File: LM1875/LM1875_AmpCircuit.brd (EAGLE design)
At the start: 59.4 x 31.7 mm, 16 parts, among them X1 22-23-2031, X2 22-23-2021, X3 22-23-2021

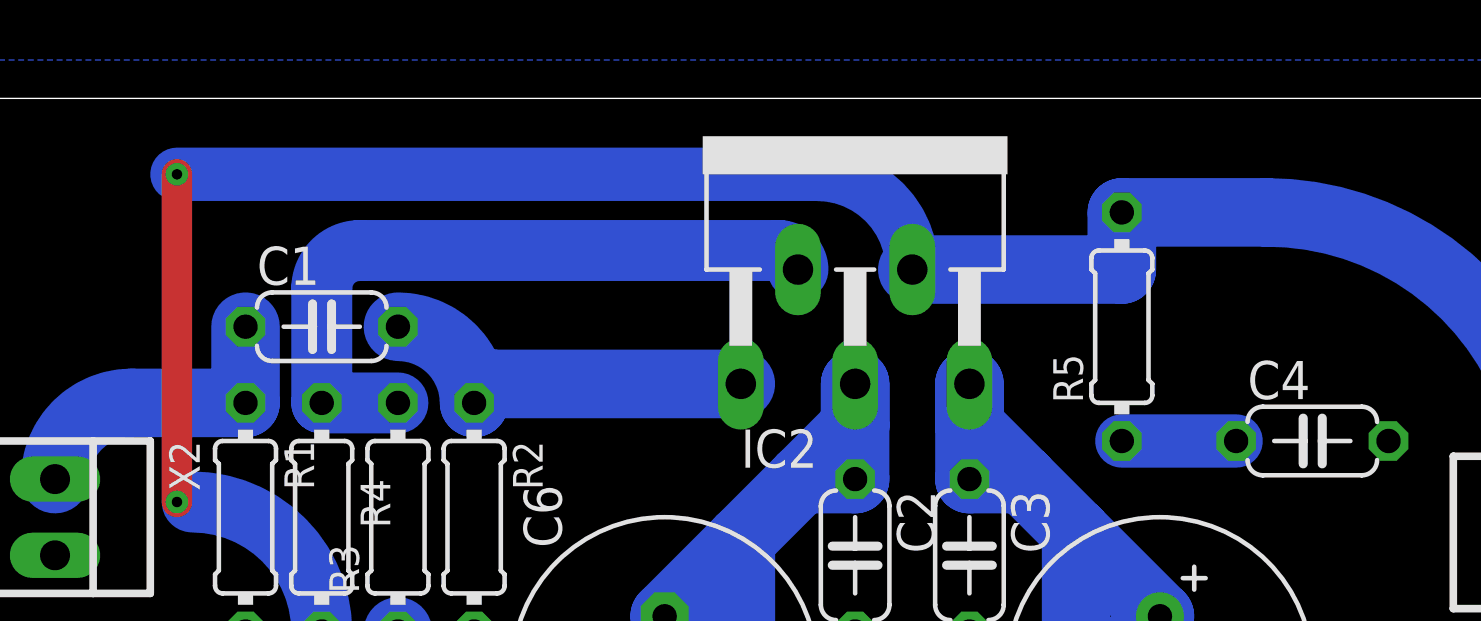
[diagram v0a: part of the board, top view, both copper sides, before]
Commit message: Edited the layout for better noise rejection
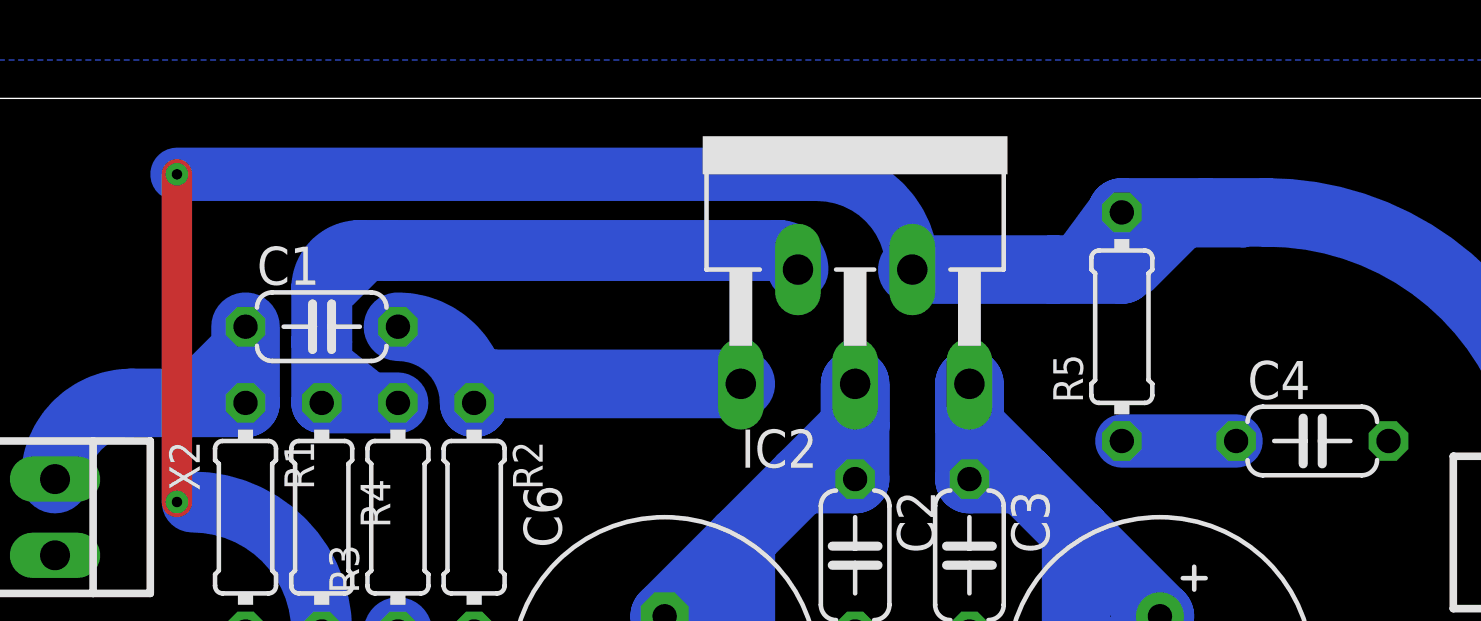
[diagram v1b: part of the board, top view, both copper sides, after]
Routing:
- net N$5: track 81.0 -> 100.2 mm
- net N$4: track 25.7 -> 31.1 mm
- net N$1: track 13.5 -> 15.9 mm
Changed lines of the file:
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@@
 <wire x1="30.48" y1="73.66" x2="31.75" y2="74.93" width="1.016" layer="16" curve="-90"/>
 <wire x1="45.72" y1="74.93" x2="46.355" y2="74.295" width="1.016" layer="16" curve="-90"/>
-<wire x1="30.48" y1="69.85" x2="30.48" y2="73.66" width="2.032" layer="16"/>
+<wire x1="30.48" y1="69.85" x2="30.48" y2="71.882" width="2.032" layer="16"/>
+<wire x1="30.48" y1="71.882" x2="30.48" y2="73.66" width="2.032" layer="16"/>
 <wire x1="30.48" y1="73.66" x2="31.75" y2="74.93" width="2.032" layer="16" curve="-90"/>
 <wire x1="46.355" y1="74.295" x2="45.72" y2="74.93" width="2.032" layer="16" curve="90"/>
-<wire x1="45.72" y1="74.93" x2="31.75" y2="74.93" width="2.032" layer="16"/>
+<wire x1="45.72" y1="74.93" x2="32.766" y2="74.93" width="2.032" layer="16"/>
+<wire x1="32.766" y1="74.93" x2="31.75" y2="74.93" width="2.032" layer="16"/>
 <wire x1="30.48" y1="69.85" x2="33.02" y2="69.85" width="2.032" layer="16"/>
+<wire x1="30.48" y1="71.882" x2="33.02" y2="69.85" width="0.8128" layer="16"/>
+<wire x1="32.766" y1="74.93" x2="31.242" y2="73.406" width="0.8128" layer="16"/>
 </signal>
 <signal name="N$5">
@@
 <via x="25.654" y="66.548" extent="1-16" drill="0.35"/>
 <wire x1="25.654" y1="77.47" x2="25.654" y2="66.548" width="1.016" layer="1"/>
-<wire x1="50.165" y1="74.295" x2="57.15" y2="74.295" width="2.286" layer="16"/>
+<wire x1="50.165" y1="74.295" x2="54.864" y2="74.295" width="2.286" layer="16"/>
+<wire x1="54.864" y1="74.295" x2="57.15" y2="74.295" width="2.286" layer="16"/>
 <wire x1="57.15" y1="74.295" x2="57.15" y2="76.2" width="2.286" layer="16"/>
-<wire x1="57.15" y1="76.2" x2="61.976" y2="76.2" width="2.286" layer="16"/>
+<wire x1="57.15" y1="76.2" x2="59.944" y2="76.2" width="2.286" layer="16"/>
+<wire x1="59.944" y1="76.2" x2="61.976" y2="76.2" width="2.286" layer="16"/>
 <wire x1="30.48" y1="62.23" x2="26.162" y2="66.548" width="2.032" layer="16" curve="90"/>
 <wire x1="25.654" y1="77.47" x2="46.99" y2="77.47" width="1.778" layer="16"/>
 <wire x1="46.99" y1="77.47" x2="50.165" y2="74.295" width="1.778" layer="16" curve="-90"/>
 <wire x1="61.976" y1="76.2" x2="71.374" y2="66.802" width="2.286" layer="16" curve="-90"/>
+<wire x1="50.165" y1="74.295" x2="53.721" y2="74.295" width="0.1524" layer="16"/>
+<wire x1="54.356" y1="74.93" x2="53.721" y2="74.295" width="0.1524" layer="16"/>
+<wire x1="54.864" y1="74.295" x2="56.642" y2="76.708" width="0.8128" layer="16"/>
+<wire x1="56.642" y1="76.708" x2="59.944" y2="76.2" width="0.8128" layer="16"/>
+<wire x1="57.15" y1="74.295" x2="59.182" y2="75.692" width="0.8128" layer="16"/>
+<wire x1="59.182" y1="75.692" x2="61.214" y2="75.438" width="0.8128" layer="16"/>
+<wire x1="61.214" y1="75.438" x2="59.436" y2="75.438" width="0.8128" layer="16"/>
+<wire x1="59.436" y1="75.438" x2="57.912" y2="73.914" width="0.8128" layer="16"/>
 </signal>
 <signal name="N$1">
@@
 <wire x1="24.13" y1="69.85" x2="27.94" y2="69.85" width="2.286" layer="16"/>
 <wire x1="27.94" y1="69.85" x2="27.94" y2="72.39" width="2.286" layer="16"/>
+<wire x1="27.94" y1="72.39" x2="27.686" y2="72.39" width="0.8128" layer="16"/>
+<wire x1="27.686" y1="72.39" x2="26.162" y2="70.866" width="0.8128" layer="16"/>
 </signal>
 <signal name="N$2">
